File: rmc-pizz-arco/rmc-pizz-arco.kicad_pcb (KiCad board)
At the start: 4 copper layers, 78.8 x 81.3 mm, 80 parts, among them J1 PZT, J2 PZT, J3 PZT, J4 PZT, J5 PZT, J6 PZT, J7 DIN-8, J8 PIZZ/ARCO, U1 OPA4191, U2 OPA4191, U3 OPA4191, U4 CD4066B, U5 CD4066B

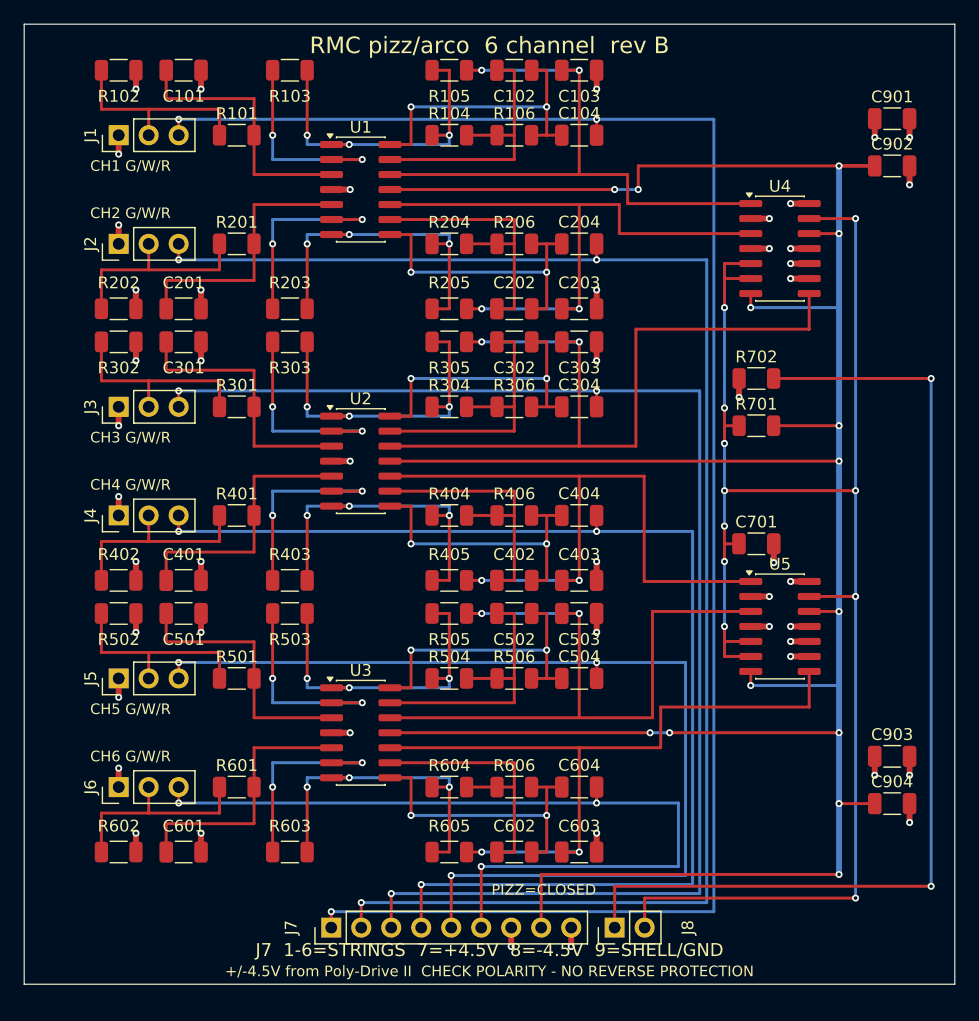
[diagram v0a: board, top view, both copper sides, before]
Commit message: Implemented latest round of recommendations from RMC
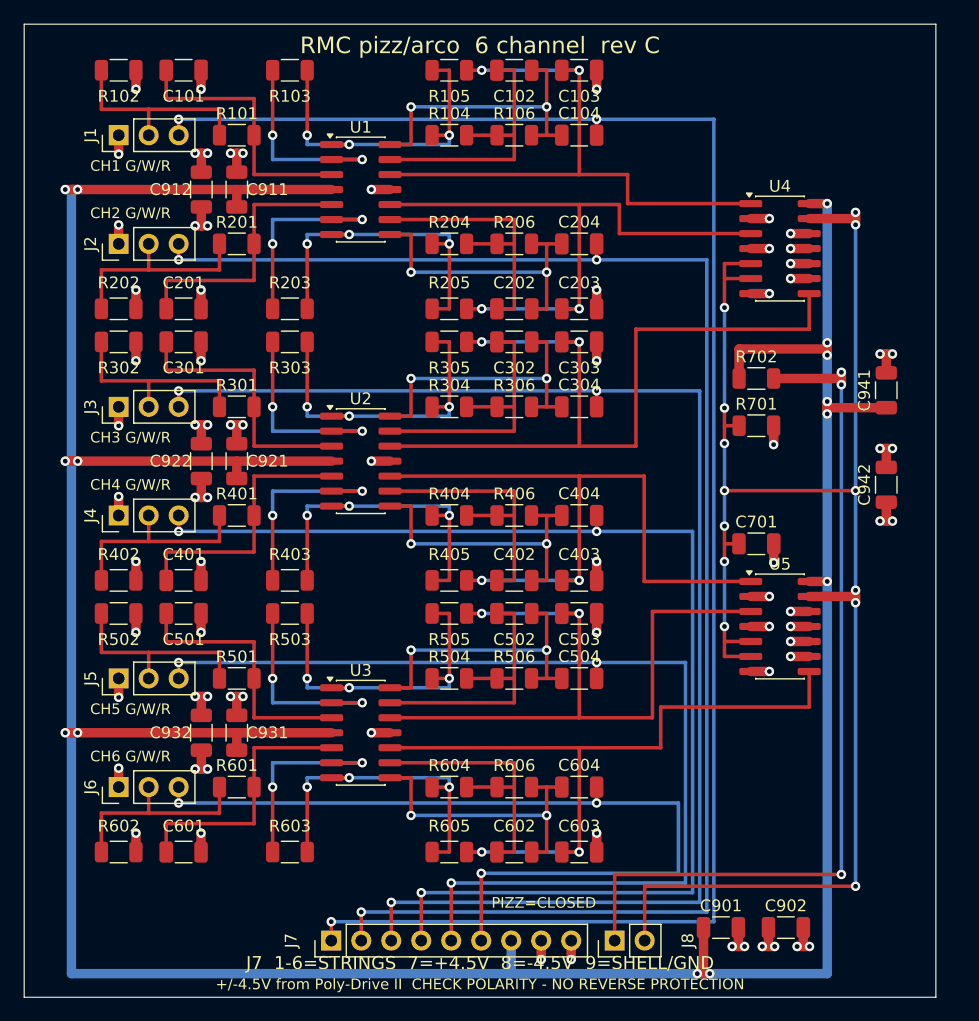
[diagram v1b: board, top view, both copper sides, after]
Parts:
- removed C903, C904: 4u7/25V, Capacitor_SMD:C_1206_3216Metric
- added C911: 4u7/25V X7R, Capacitor_SMD:C_1206_3216Metric, F.Cu at (18.0, 14.0)
- added C912: 4u7/25V X7R, Capacitor_SMD:C_1206_3216Metric, F.Cu at (15.0, 14.0)
- added C921: 4u7/25V X7R, Capacitor_SMD:C_1206_3216Metric, F.Cu at (18.0, 37.0)
- added C922: 4u7/25V X7R, Capacitor_SMD:C_1206_3216Metric, F.Cu at (15.0, 37.0)
- added C931: 4u7/25V X7R, Capacitor_SMD:C_1206_3216Metric, F.Cu at (18.0, 60.0)
- added C932: 4u7/25V X7R, Capacitor_SMD:C_1206_3216Metric, F.Cu at (15.0, 60.0)
- added C941: 4u7/25V X7R, Capacitor_SMD:C_1206_3216Metric, F.Cu at (73.0, 31.0)
- added C942: 4u7/25V X7R, Capacitor_SMD:C_1206_3216Metric, F.Cu at (73.0, 39.0)
- C901, C902: value 4u7/25V -> 4u7/25V X7R
- moved C901 70.0 mm to (59.0, 76.5)
- moved C902 65.1 mm to (64.5, 76.5)
- moved J7 1.10 mm to (26.0, 77.6)
- moved J8 1.10 mm to (50.0, 77.6)
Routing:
- net V+: track 14.3 -> 297.1 mm, vias 9 -> 14
- net V-: track 242.8 -> 27.5 mm, vias 14 -> 19
- net AGND: track 63.7 -> 83.8 mm, vias 40 -> 56
- net SW_TOG: track 86.6 -> 73.6 mm, vias 2 -> 3
- net SW_CTL: track 141.5 -> 144.7 mm, vias 11 -> 13
- net OUT3: track 118.4 -> 119.5 mm
- net OUT1: track 148.9 -> 150.0 mm
- net OUT6: track 72.3 -> 73.4 mm
- net OUT5: track 87.9 -> 89.0 mm
- net OUT4: track 102.8 -> 103.8 mm
- net OUT2: track 133.2 -> 134.3 mm
- added copper zone on In2.Cu, net V-
- removed copper zone on In2.Cu, net V+
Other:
- board size 78.8 x 81.3 mm -> 77.2 x 82.4 mm
- board text added: "RMC pizz/arco 6 channel rev C"
- board text removed: "RMC pizz/arco 6 channel rev B"

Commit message: Implemented latest round of recommendations from RMC
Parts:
- removed R103, R203, R303, R403, R503, R603: 1k, Resistor_SMD:R_1206_3216Metric
- moved C602 8.67 mm to (34.8, 64.6)
- moved C102 8.67 mm to (34.8, 9.40)
- moved C202 8.67 mm to (34.8, 18.6)
- moved C302 8.67 mm to (34.8, 32.4)
- moved C402 8.67 mm to (34.8, 41.6)
- moved C502 8.67 mm to (34.8, 55.4)
- moved R604 5.63 mm to (34.8, 70.1), turned to 180 degrees
- moved R104 5.63 mm to (34.8, 3.90), turned to 180 degrees
- moved R204 5.63 mm to (34.8, 24.1), turned to 180 degrees
- moved R304 5.63 mm to (34.8, 26.9), turned to 180 degrees
- moved R404 5.63 mm to (34.8, 47.1), turned to 180 degrees
- moved R504 5.63 mm to (34.8, 49.9), turned to 180 degrees
- moved R105 3.80 mm to (39.8, 3.90)
- moved R205 3.80 mm to (39.8, 24.1)
- moved R305 3.80 mm to (39.8, 26.9)
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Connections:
- U1 pad 2: BUFFB1 -> BUFOUT1
- U1 pad 6: BUFFB2 -> BUFOUT2
- U2 pad 2: BUFFB3 -> BUFOUT3
- U2 pad 6: BUFFB4 -> BUFOUT4
- U3 pad 2: BUFFB5 -> BUFOUT5
- U3 pad 6: BUFFB6 -> BUFOUT6
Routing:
- net BUFFB5: track 17.7 -> 0.00 mm, vias 2 -> 0
- net BUFFB4: track 17.7 -> 0.00 mm, vias 2 -> 0
- net BUFFB3: track 17.7 -> 0.00 mm, vias 2 -> 0
- net BUFFB2: track 17.7 -> 0.00 mm, vias 2 -> 0
- net BUFFB1: track 17.7 -> 0.00 mm, vias 2 -> 0
- net BUFFB6: track 17.7 -> 0.00 mm, vias 2 -> 0
- net BUFOUT2: track 29.0 -> 19.9 mm, vias 3 -> 2
- net BUFOUT5: track 29.0 -> 19.9 mm, vias 3 -> 2
- net BUFOUT4: track 29.0 -> 19.9 mm, vias 3 -> 2
- net BUFOUT1: track 29.0 -> 19.9 mm, vias 3 -> 2
- net BUFOUT6: track 29.0 -> 19.9 mm, vias 3 -> 2
- net BUFOUT3: track 29.0 -> 19.9 mm, vias 3 -> 2
- net SWN6: track 61.8 -> 54.3 mm, vias 2 -> 0
- net SWN5: track 59.4 -> 51.9 mm, vias 2 -> 0
- net SWN4: track 59.3 -> 51.8 mm, vias 2 -> 0
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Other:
- board text added: "RMC pizz/arco 6 channel rev D"
- board text removed: "RMC pizz/arco 6 channel rev C"
